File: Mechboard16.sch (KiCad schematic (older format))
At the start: 154 parts, among them CN1 CONN_C16, CN2 CONN_+4, SW0:0 KEY_DEL, SW0:1 KEY_RET, SW0:2 KEY_PND, SW0:3 KEY_HLP, SW0:4 KEY_F1, SW0:5 KEY_F2, SW0:6 KEY_F3, SW0:7 KEY_AT, SW1:0 KEY_3, SW1:1 KEY_W, SW1:2 KEY_A, SW1:3 KEY_4, SW1:4 KEY_Z, SW1:5 KEY_S, SW1:6 KEY_E, SW1:7 KEY_LSH, SW1B:7 KEY_RSH, SW1C:7 KEY_CLK, SW2:0 KEY_5, SW2:1 KEY_R, SW2:2 KEY_D, SW2:3 KEY_6, SW2:4 KEY_C, SW2:5 KEY_F, SW2:6 KEY_T, SW2:7 KEY_X, SW3:0 KEY_7, SW3:1 KEY_Y, SW3:2 KEY_G, SW3:3 KEY_8, SW3:4 KEY_B, SW3:5 KEY_H, SW3:6 KEY_U, SW3:7 KEY_V, SW4:0 KEY_9, SW4:1 KEY_I, SW4:2 KEY_J, SW4:3 KEY_0, SW4:4 KEY_M, SW4:5 KEY_K, SW4:6 KEY_O, SW4:7 KEY_N, SW5:0 KEY_DN, SW5:1 KEY_P, SW5:2 KEY_L, SW5:3 KEY_UP, SW5:4 KEY_DOT, SW5:5 KEY_COL, SW5:6 KEY_MIN, SW5:7 KEY_COM, SW6:0 KEY_LF, SW6:1 KEY_AST, SW6:2 KEY_SEM, SW6:3 KEY_RT, SW6:4 KEY_ESC, SW6:5 KEY_EQ, SW6:6 KEY_PLS, SW6:7 KEY_SLA, SW7:0 KEY_1, SW7:1 KEY_CLR, SW7:2 KEY_CTL, SW7:3 KEY_2, SW7:4 KEY_SPC, SW7:5 KEY_CMD, SW7:6 KEY_Q, SW7:7 KEY_RUN, U1 4066, U2 NE555

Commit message: Begin adding Kailh MX sockets
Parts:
- SW0:0, SW0:2, SW0:7, SW1:0, SW1:1, SW1:2, SW1:3, SW1:4, SW1:5, SW1:6, SW1C:7, SW2:0, SW2:1, SW2:2, SW2:3, SW2:4, SW2:5, SW2:6, SW2:7, SW3:0, SW3:1, SW3:2, SW3:3, SW3:4, SW3:5, SW3:6, SW3:7, SW4:0, SW4:1, SW4:2, SW4:3, SW4:4, SW4:5, SW4:6, SW4:7, SW5:0, SW5:1, SW5:2, SW5:3, SW5:4, SW5:5, SW5:6, SW5:7, SW6:0, SW6:1, SW6:2, SW6:3, SW6:4, SW6:5, SW6:6, SW6:7, SW7:0, SW7:1, SW7:3, SW7:5, SW7:6, SW7:7: footprint Mechboard16:SW_Cherry_MX_PCB_1.00u -> Mechboard16:SW_Hotswap_Kailh_MX_1.00u

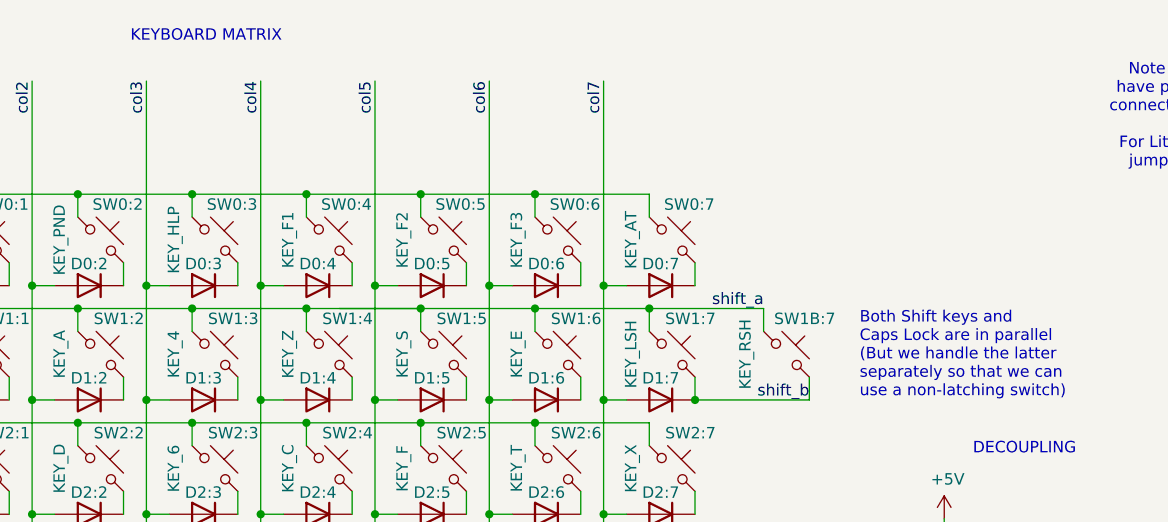
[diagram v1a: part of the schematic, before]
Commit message: Switch to MX sockets
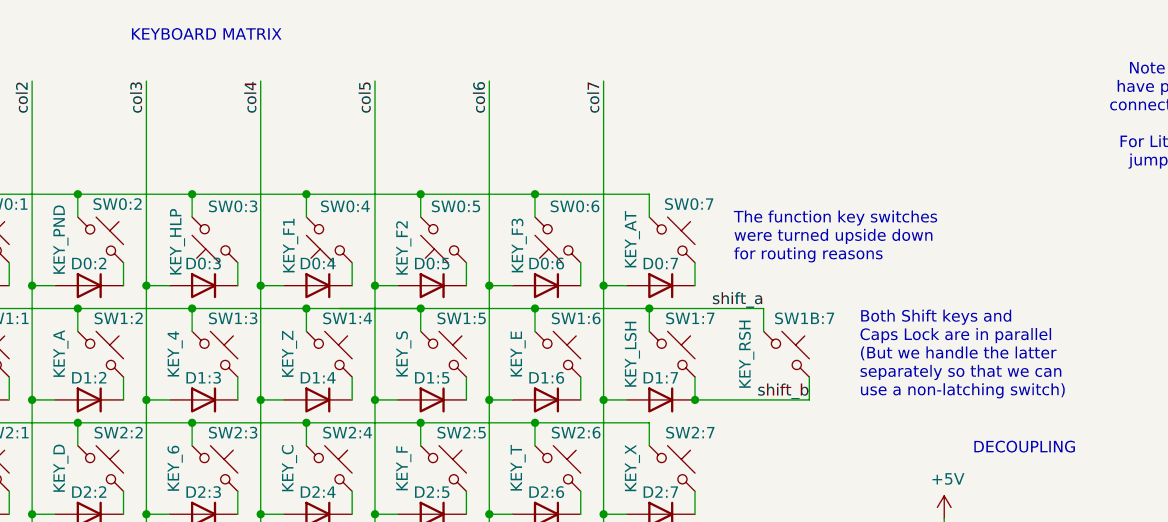
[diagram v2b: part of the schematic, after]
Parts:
- SW0:1: footprint Mechboard16:SW_Cherry_MX_PCB_2.00u -> Mechboard16:SW_Hotswap_Kailh_MX_2.00u
- SW0:3, SW0:4, SW0:5, SW0:6, SW1:7, SW1B:7, SW7:2: footprint Mechboard16:SW_Cherry_MX_PCB_1.50u_OffsetR -> Mechboard16:SW_Hotswap_Kailh_MX_1.50u_OffsetR
- SW7:1: footprint Mechboard16:SW_Hotswap_Kailh_MX_1.00u -> Mechboard16:SW_Hotswap_Kailh_MX_1.50u_OffsetL
- SW7:4: footprint Mechboard16:SW_Cherry_MX_PCB_9.00u -> Mechboard16:SW_Hotswap_Kailh_MX_9.00u
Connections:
- net row0: now also SW0:3.2, SW0:4.2, SW0:5.2, SW0:6.2; no longer SW0:3.1, SW0:4.1, SW0:5.1, SW0:6.1
- net at D0:3.1 (K): now also SW0:3.1; no longer SW0:3.2
- net at D0:4.1 (K): now also SW0:4.1; no longer SW0:4.2
- net at D0:5.1 (K): now also SW0:5.1; no longer SW0:5.2
- net at D0:6.1 (K): now also SW0:6.1; no longer SW0:6.2
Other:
- note added: "The function key switches\nwere turned upside down\nfor routing reasons"
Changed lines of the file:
@@
 F 0 "SW0:1" H 2350 1690 50  0000 C CNN
 F 1 "KEY_RET" V 2095 1535 50  0000 C CNN
-F 2 "Mechboard16:SW_Cherry_MX_PCB_2.00u" H 2275 1535 50  0001 C CNN
+F 2 "Mechboard16:SW_Hotswap_Kailh_MX_2.00u" H 2275 1535 50  0001 C CNN
 F 3 "~" H 2275 1535 50  0001 C CNN
 	1    2275 1535
@@
 F 0 "SW7:1" H 2355 5190 50  0000 C CNN
 F 1 "KEY_CLR" V 2095 5035 50  0000 C CNN
-F 2 "Mechboard16:SW_Hotswap_Kailh_MX_1.00u" H 2275 5035 50  0001 C CNN
+F 2 "Mechboard16:SW_Hotswap_Kailh_MX_1.50u_OffsetL" H 2275 5035 50  0001 C CNN
 F 3 "~" H 2275 5035 50  0001 C CNN
 	1    2275 5035
@@
 F 0 "SW7:2" H 2855 5190 50  0000 C CNN
 F 1 "KEY_CTL" V 2595 5035 50  0000 C CNN
-F 2 "Mechboard16:SW_Cherry_MX_PCB_1.50u_OffsetR" H 2775 5035 50  0001 C CNN
+F 2 "Mechboard16:SW_Hotswap_Kailh_MX_1.50u_OffsetR" H 2775 5035 50  0001 C CNN
 F 3 "~" H 2775 5035 50  0001 C CNN
 	1    2775 5035
@@
 Wire Wire Line
 	2475 2735 2475 3235
-$Comp
-L Switch:SW_Push_45deg SW0:3
-U 1 1 6580578A
-P 3275 1535
-F 0 "SW0:3" H 3350 1690 50  0000 C CNN
-F 1 "KEY_HLP" V 3095 1535 50  0000 C CNN
-F 2 "Mechboard16:SW_Cherry_MX_PCB_1.50u_OffsetR" H 3275 1535 50  0001 C CNN
-F 3 "~" H 3275 1535 50  0001 C CNN
-	1    3275 1535
-	1    0    0    -1
-$EndComp
-$Comp
-L Device:D D0:3
-U 1 1 65805792
-P 3225 1735
-F 0 "D0:3" H 3225 1830 50  0000 C CNN
-F 1 "1n4148" H 3225 1861 50  0001 C CNN
-F 2 "Diode_SMD:D_SOD-323_HandSoldering" H 3225 1735 50  0001 C CNN
-F 3 "~" H 3225 1735 50  0001 C CNN
-F 4 "C2128" H 3225 1735 50  0001 C CNN "LCSC"
-	1    3225 1735
-	-1   0    0    -1
-$EndComp
 Wire Wire Line
 	3375 1735 3375 1635
@@
 U 1 1 6581A489
 P 3775 1535
-F 0 "SW0:4" H 3850 1690 50  0000 C CNN
-F 1 "KEY_F1" V 3595 1535 50  0000 C CNN
-F 2 "Mechboard16:SW_Cherry_MX_PCB_1.50u_OffsetR" H 3775 1535 50  0001 C CNN
+F 0 "SW0:4" H 3705 1390 50  0000 C CNN
+F 1 "KEY_F1" V 3950 1560 50  0000 C CNN
+F 2 "Mechboard16:SW_Hotswap_Kailh_MX_1.50u_OffsetR" H 3775 1535 50  0001 C CNN
 F 3 "~" H 3775 1535 50  0001 C CNN
 	1    3775 1535
-	1    0    0    -1
+	-1   0    0    1
 $EndComp
 Wire Wire Line
@@
 F 0 "SW7:4" H 3855 5190 50  0000 C CNN
 F 1 "KEY_SPC" V 3595 5035 50  0000 C CNN
-F 2 "Mechboard16:SW_Cherry_MX_PCB_9.00u" H 3775 5035 50  0001 C CNN
+F 2 "Mechboard16:SW_Hotswap_Kailh_MX_9.00u" H 3775 5035 50  0001 C CNN
 F 3 "~" H 3775 5035 50  0001 C CNN
 	1    3775 5035
@@
 U 1 1 65838F0C
 P 4275 1535
-F 0 "SW0:5" H 4350 1690 50  0000 C CNN
-F 1 "KEY_F2" V 4095 1535 50  0000 C CNN
-F 2 "Mechboard16:SW_Cherry_MX_PCB_1.50u_OffsetR" H 4275 1535 50  0001 C CNN
+F 0 "SW0:5" H 4220 1390 50  0000 C CNN
+F 1 "KEY_F2" V 4455 1570 50  0000 C CNN
+F 2 "Mechboard16:SW_Hotswap_Kailh_MX_1.50u_OffsetR" H 4275 1535 50  0001 C CNN
 F 3 "~" H 4275 1535 50  0001 C CNN
 	1    4275 1535
-	1    0    0    -1
+	-1   0    0    1
 $EndComp
 Wire Wire Line
@@
 U 1 1 6586B7F1
 P 4775 1535
-F 0 "SW0:6" H 4850 1690 50  0000 C CNN
-F 1 "KEY_F3" V 4595 1535 50  0000 C CNN
-F 2 "Mechboard16:SW_Cherry_MX_PCB_1.50u_OffsetR" H 4775 1535 50  0001 C CNN
+F 0 "SW0:6" H 4700 1390 50  0000 C CNN
+F 1 "KEY_F3" V 4950 1560 50  0000 C CNN
+F 2 "Mechboard16:SW_Hotswap_Kailh_MX_1.50u_OffsetR" H 4775 1535 50  0001 C CNN
 F 3 "~" H 4775 1535 50  0001 C CNN
 	1    4775 1535
-	1    0    0    -1
+	-1   0    0    1
 $EndComp
 Wire Wire Line
@@
 F 0 "SW1:7" H 5355 2190 50  0000 C CNN
 F 1 "KEY_LSH" V 5095 2035 50  0000 C CNN
-F 2 "Mechboard16:SW_Cherry_MX_PCB_1.50u_OffsetR" H 5275 2035 50  0001 C CNN
+F 2 "Mechboard16:SW_Hotswap_Kailh_MX_1.50u_OffsetR" H 5275 2035 50  0001 C CNN
 F 3 "~" H 5275 2035 50  0001 C CNN
 	1    5275 2035
@@
 F 0 "SW1B:7" H 5855 2190 50  0000 C CNN
 F 1 "KEY_RSH" V 5595 2035 50  0000 C CNN
-F 2 "Mechboard16:SW_Cherry_MX_PCB_1.50u_OffsetR" H 5775 2035 50  0001 C CNN
+F 2 "Mechboard16:SW_Hotswap_Kailh_MX_1.50u_OffsetR" H 5775 2035 50  0001 C CNN
 F 3 "~" H 5775 2035 50  0001 C CNN
 	1    5775 2035
@@
 	-1   0    0    -1
 $EndComp
+$Comp
+L Switch:SW_Push_45deg SW0:3
+U 1 1 6580578A
+P 3275 1535
+F 0 "SW0:3" H 3195 1390 50  0000 C CNN
+F 1 "KEY_HLP" V 3445 1545 50  0000 C CNN
+F 2 "Mechboard16:SW_Hotswap_Kailh_MX_1.50u_OffsetR" H 3275 1535 50  0001 C CNN
+F 3 "~" H 3275 1535 50  0001 C CNN
+	1    3275 1535
+	-1   0    0    1
+$EndComp
+$Comp
+L Device:D D0:3
+U 1 1 65805792
+P 3225 1735
+F 0 "D0:3" H 3225 1830 50  0000 C CNN
+F 1 "1n4148" H 3225 1861 50  0001 C CNN
+F 2 "Diode_SMD:D_SOD-323_HandSoldering" H 3225 1735 50  0001 C CNN
+F 3 "~" H 3225 1735 50  0001 C CNN
+F 4 "C2128" H 3225 1735 50  0001 C CNN "LCSC"
+	1    3225 1735
+	-1   0    0    -1
+$EndComp
+Text Notes 5545 1635 0    50   ~ 0
+The function key switches\nwere turned upside down\nfor routing reasons
 Wire Bus Line
 	1715 5975 1715 6805

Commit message: Turning sockets upside-down and switching to SMD leds
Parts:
- SW7:1: footprint Mechboard16:SW_Hotswap_Kailh_MX_1.50u_OffsetL -> Mechboard16:SW_Hotswap_Kailh_MX_1.50u_OffsetR
- SW7:2: footprint Mechboard16:SW_Hotswap_Kailh_MX_1.50u_OffsetR -> Mechboard16:SW_Hotswap_Kailh_MX_1.50u_OffsetL
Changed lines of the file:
@@
 F 0 "SW7:1" H 2355 5190 50  0000 C CNN
 F 1 "KEY_CLR" V 2095 5035 50  0000 C CNN
-F 2 "Mechboard16:SW_Hotswap_Kailh_MX_1.50u_OffsetL" H 2275 5035 50  0001 C CNN
+F 2 "Mechboard16:SW_Hotswap_Kailh_MX_1.50u_OffsetR" H 2275 5035 50  0001 C CNN
 F 3 "~" H 2275 5035 50  0001 C CNN
 	1    2275 5035
@@
 F 0 "SW7:2" H 2855 5190 50  0000 C CNN
 F 1 "KEY_CTL" V 2595 5035 50  0000 C CNN
-F 2 "Mechboard16:SW_Hotswap_Kailh_MX_1.50u_OffsetR" H 2775 5035 50  0001 C CNN
+F 2 "Mechboard16:SW_Hotswap_Kailh_MX_1.50u_OffsetL" H 2775 5035 50  0001 C CNN
 F 3 "~" H 2775 5035 50  0001 C CNN
 	1    2775 5035

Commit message: Most horizontal key and led connections done
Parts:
- LD1C:7: footprint LED_THT:LED_D3.0mm -> Mechboard16:LED_MX_6028R
- SW1:7, SW1B:7: footprint Mechboard16:SW_Hotswap_Kailh_MX_1.50u_OffsetR -> Mechboard16:SW_Hotswap_Kailh_MX_1.50u_OffsetL
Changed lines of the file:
@@
 F 0 "SW1:7" H 5355 2190 50  0000 C CNN
 F 1 "KEY_LSH" V 5095 2035 50  0000 C CNN
-F 2 "Mechboard16:SW_Hotswap_Kailh_MX_1.50u_OffsetR" H 5275 2035 50  0001 C CNN
+F 2 "Mechboard16:SW_Hotswap_Kailh_MX_1.50u_OffsetL" H 5275 2035 50  0001 C CNN
 F 3 "~" H 5275 2035 50  0001 C CNN
 	1    5275 2035
@@
 F 0 "SW1B:7" H 5855 2190 50  0000 C CNN
 F 1 "KEY_RSH" V 5595 2035 50  0000 C CNN
-F 2 "Mechboard16:SW_Hotswap_Kailh_MX_1.50u_OffsetR" H 5775 2035 50  0001 C CNN
+F 2 "Mechboard16:SW_Hotswap_Kailh_MX_1.50u_OffsetL" H 5775 2035 50  0001 C CNN
 F 3 "~" H 5775 2035 50  0001 C CNN
 	1    5775 2035
@@
 F 0 "LD1C:7" V 9709 5752 50  0000 R CNN
 F 1 "LED_CLK" V 9618 5752 50  0000 R CNN
-F 2 "LED_THT:LED_D3.0mm" H 9670 5870 50  0001 C CNN
+F 2 "Mechboard16:LED_MX_6028R" H 9670 5870 50  0001 C CNN
 F 3 "~" H 9670 5870 50  0001 C CNN
 	1    9670 5870

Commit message: Routing... Routing... Routing...
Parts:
- SW0:3, SW0:4, SW0:5, SW0:6: footprint Mechboard16:SW_Hotswap_Kailh_MX_1.50u_OffsetR -> Mechboard16:SW_Hotswap_Kailh_MX_1.50u_OffsetL
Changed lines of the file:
@@
 F 0 "SW0:4" H 3705 1390 50  0000 C CNN
 F 1 "KEY_F1" V 3950 1560 50  0000 C CNN
-F 2 "Mechboard16:SW_Hotswap_Kailh_MX_1.50u_OffsetR" H 3775 1535 50  0001 C CNN
+F 2 "Mechboard16:SW_Hotswap_Kailh_MX_1.50u_OffsetL" H 3775 1535 50  0001 C CNN
 F 3 "~" H 3775 1535 50  0001 C CNN
 	1    3775 1535
@@
 F 0 "SW0:5" H 4220 1390 50  0000 C CNN
 F 1 "KEY_F2" V 4455 1570 50  0000 C CNN
-F 2 "Mechboard16:SW_Hotswap_Kailh_MX_1.50u_OffsetR" H 4275 1535 50  0001 C CNN
+F 2 "Mechboard16:SW_Hotswap_Kailh_MX_1.50u_OffsetL" H 4275 1535 50  0001 C CNN
 F 3 "~" H 4275 1535 50  0001 C CNN
 	1    4275 1535
@@
 F 0 "SW0:6" H 4700 1390 50  0000 C CNN
 F 1 "KEY_F3" V 4950 1560 50  0000 C CNN
-F 2 "Mechboard16:SW_Hotswap_Kailh_MX_1.50u_OffsetR" H 4775 1535 50  0001 C CNN
+F 2 "Mechboard16:SW_Hotswap_Kailh_MX_1.50u_OffsetL" H 4775 1535 50  0001 C CNN
 F 3 "~" H 4775 1535 50  0001 C CNN
 	1    4775 1535
@@
 F 0 "SW0:3" H 3195 1390 50  0000 C CNN
 F 1 "KEY_HLP" V 3445 1545 50  0000 C CNN
-F 2 "Mechboard16:SW_Hotswap_Kailh_MX_1.50u_OffsetR" H 3275 1535 50  0001 C CNN
+F 2 "Mechboard16:SW_Hotswap_Kailh_MX_1.50u_OffsetL" H 3275 1535 50  0001 C CNN
 F 3 "~" H 3275 1535 50  0001 C CNN
 	1    3275 1535

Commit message: -30
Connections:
- net row0: now also SW0:3.1, SW0:4.1, SW0:5.1, SW0:6.1; no longer SW0:3.2, SW0:4.2, SW0:5.2, SW0:6.2
- net at D0:3.1 (K): now also SW0:3.2; no longer SW0:3.1
- net at D0:4.1 (K): now also SW0:4.2; no longer SW0:4.1
- net at D0:5.1 (K): now also SW0:5.2; no longer SW0:5.1
- net at D0:6.1 (K): now also SW0:6.2; no longer SW0:6.1
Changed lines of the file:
@@
 Wire Wire Line
 	2975 2735 2975 3235
-$Comp
-L Switch:SW_Push_45deg SW0:4
-U 1 1 6581A489
-P 3775 1535
-F 0 "SW0:4" H 3705 1390 50  0000 C CNN
-F 1 "KEY_F1" V 3950 1560 50  0000 C CNN
-F 2 "Mechboard16:SW_Hotswap_Kailh_MX_1.50u_OffsetL" H 3775 1535 50  0001 C CNN
-F 3 "~" H 3775 1535 50  0001 C CNN
-	1    3775 1535
-	-1   0    0    1
-$EndComp
 Wire Wire Line
 	3675 1435 3675 1335
@@
 U 1 1 65838F0C
 P 4275 1535
-F 0 "SW0:5" H 4220 1390 50  0000 C CNN
-F 1 "KEY_F2" V 4455 1570 50  0000 C CNN
+F 0 "SW0:5" H 4350 1685 50  0000 C CNN
+F 1 "KEY_F2" V 4100 1520 50  0000 C CNN
 F 2 "Mechboard16:SW_Hotswap_Kailh_MX_1.50u_OffsetL" H 4275 1535 50  0001 C CNN
 F 3 "~" H 4275 1535 50  0001 C CNN
 	1    4275 1535
-	-1   0    0    1
+	1    0    0    -1
 $EndComp
 Wire Wire Line
@@
 U 1 1 6586B7F1
 P 4775 1535
-F 0 "SW0:6" H 4700 1390 50  0000 C CNN
-F 1 "KEY_F3" V 4950 1560 50  0000 C CNN
+F 0 "SW0:6" H 4850 1685 50  0000 C CNN
+F 1 "KEY_F3" V 4600 1520 50  0000 C CNN
 F 2 "Mechboard16:SW_Hotswap_Kailh_MX_1.50u_OffsetL" H 4775 1535 50  0001 C CNN
 F 3 "~" H 4775 1535 50  0001 C CNN
 	1    4775 1535
-	-1   0    0    1
+	1    0    0    -1
 $EndComp
 Wire Wire Line
@@
 U 1 1 6580578A
 P 3275 1535
-F 0 "SW0:3" H 3195 1390 50  0000 C CNN
-F 1 "KEY_HLP" V 3445 1545 50  0000 C CNN
+F 0 "SW0:3" H 3350 1685 50  0000 C CNN
+F 1 "KEY_HLP" V 3100 1535 50  0000 C CNN
 F 2 "Mechboard16:SW_Hotswap_Kailh_MX_1.50u_OffsetL" H 3275 1535 50  0001 C CNN
 F 3 "~" H 3275 1535 50  0001 C CNN
 	1    3275 1535
-	-1   0    0    1
+	1    0    0    -1
 $EndComp
 $Comp
@@
 Wire Bus Line
 	2190 5975 2190 6805
+$Comp
+L Switch:SW_Push_45deg SW0:4
+U 1 1 6581A489
+P 3775 1535
+F 0 "SW0:4" H 3855 1685 50  0000 C CNN
+F 1 "KEY_F1" V 3600 1510 50  0000 C CNN
+F 2 "Mechboard16:SW_Hotswap_Kailh_MX_1.50u_OffsetL" H 3775 1535 50  0001 C CNN
+F 3 "~" H 3775 1535 50  0001 C CNN
+	1    3775 1535
+	1    0    0    -1
+$EndComp
 $EndSCHEMATC

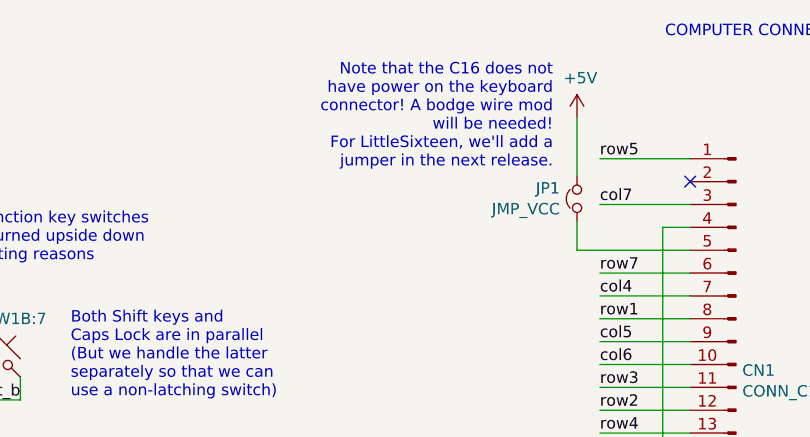
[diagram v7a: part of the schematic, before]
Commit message: Remove power jumper
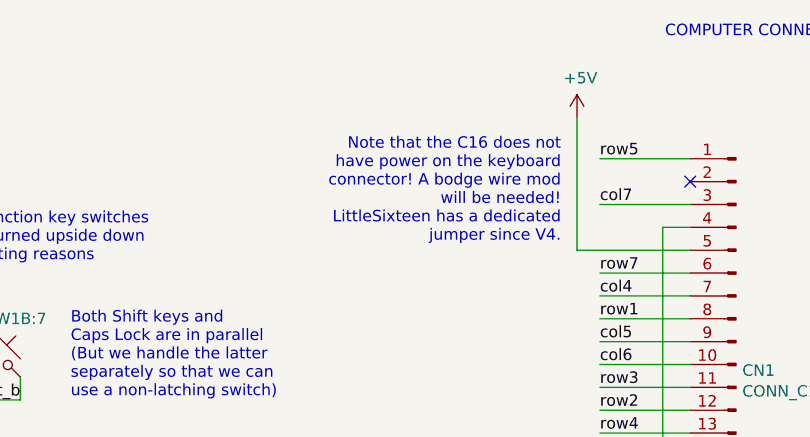
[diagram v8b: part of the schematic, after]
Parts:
- removed JP1: JMP_VCC, Jumper:SolderJumper-2_P1.3mm_Bridged_RoundedPad1.0x1.5mm, symbol Device:Jumper_NC_Small
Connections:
- net +5V: now also CN1.5 (Pin_5)
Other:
- note added: "Note that the C16 does not\nhave power on the keyboard\nconnector! A bodge wire mod\nwill be needed!\nLittleSixteen has a dedicated\njumper since V4."
- note removed: "Note that the C16 does not\nhave power on the keyboard\nconnector! A bodge wire mod\nwill be needed!\nFor LittleSixteen, we'll add a\njumper in the next release."
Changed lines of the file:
@@
 Sheet 1 2
 Title "Mechboard16"
-Date "2024-01-08"
+Date "2025-12-22"
 Rev "1git"
 Comp "SukkoPera"
@@
 	1    0    0    -1
 $EndComp
-Text Label 8410 1680 0    50   ~ 0
-row7
 Text Label 8410 1780 0    50   ~ 0
 col4
@@
 row0
 NoConn ~ 8805 3080
-$Comp
-L Device:Jumper_NC_Small JP1
-U 1 1 666B3C47
-P 8310 1355
-F 0 "JP1" V 8356 1430 50  0000 L CNN
-F 1 "JMP_VCC" V 8265 1430 50  0000 L CNN
-F 2 "Jumper:SolderJumper-2_P1.3mm_Bridged_RoundedPad1.0x1.5mm" H 8310 1355 50  0001 C CNN
-F 3 "~" H 8310 1355 50  0001 C CNN
-	1    8310 1355
-	0    -1   -1   0
-$EndComp
 Wire Wire Line
 	8805 1580 8310 1580
-Wire Wire Line
-	8310 1580 8310 1455
-Wire Wire Line
-	8310 1255 8310 1000
 $Comp
 L power:+5V #PWR01
@@
 Wire Wire Line
 	7245 3235 7245 3175
-Text Notes 8205 1225 2    50   ~ 0
-Note that the C16 does not\nhave power on the keyboard\nconnector! A bodge wire mod\nwill be needed!\nFor LittleSixteen, we'll add a\njumper in the next release.
+Text Notes 8240 1550 2    50   ~ 0
+Note that the C16 does not\nhave power on the keyboard\nconnector! A bodge wire mod\nwill be needed!\nLittleSixteen has a dedicated\njumper since V4.
 $Comp
 L Mechanical:MountingHole H4
@@
 	1    0    0    -1
 $EndComp
+Text Label 8410 1680 0    50   ~ 0
+row7
+Wire Wire Line
+	8310 1000 8310 1580
 Wire Bus Line
 	1715 5975 1715 6805
